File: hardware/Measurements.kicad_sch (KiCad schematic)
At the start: 4 parts, among them IC1 MCP1501-10E_SN

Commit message: minor changes
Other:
- note removed: "first stage lowpass filter"
- note removed: "second stage lowpass filter"
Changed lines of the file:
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@@
     (effects (font (size 5 5) (thickness 1) bold) (justify left bottom))
-  )
-  (text "second stage lowpass filter" (at 107.95 146.05 0)
-    (effects (font (size 1.27 1.27)) (justify left bottom))
   )
   (text "Sensor Reference" (at 198.755 29.21 0)
@@
     (effects (font (size 5 5) (thickness 1) bold) (justify left bottom))
   )
-  (text "first stage lowpass filter" (at 59.055 146.05 0)
-    (effects (font (size 1.27 1.27)) (justify left bottom))
-  )
   (global_label "HV_CAR+" (shape input) (at 74.295 74.295 180) (fields_autoplaced)

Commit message: pcb update
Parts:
- gave numbers to parts that had none: 1
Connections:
- net CUR_SENS_SIG: now also IC6.3 (+); no longer IC6.1 (NC)
- net SENSOR_SIGNAL_MCU: now also IC6.1; no longer IC6.2
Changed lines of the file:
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@@
   (symbol (lib_id "ADA4505-1ARJZ-R7:ADA4505-1ARJZ-R7") (at 86.995 162.56 0) (unit 1)
     (in_bom yes) (on_board yes)
-    (property "Reference" "IC?" (id 0) (at 94.615 155.575 0))
+    (property "Reference" "IC6" (id 0) (at 94.615 155.575 0))
     (property "Value" "ADA4505-1ARJZ-R7" (id 1) (at 99.06 157.48 0))
     (property "Footprint" "SOT95P280X145-5N" (id 2) (at 108.585 160.02 0)
@@
       (effects (font (size 1.27 1.27)) (justify left) hide)
     )
-    (pin "1")
+    (pin "3")
     (pin "1")
     (pin "2")
-    (pin "2")
+    (pin "1")
     (pin "4")
     (pin "5")
@@
   (symbol (lib_id "power:GND") (at 85.725 172.72 0) (unit 1)
     (in_bom yes) (on_board yes)
-    (property "Reference" "#PWR?" (id 0) (at 85.725 179.07 0)
+    (property "Reference" "#PWR0183" (id 0) (at 85.725 179.07 0)
       (effects (font (size 1.27 1.27)) hide)
     )
@@
   (symbol (lib_id "power:+3.3V") (at 85.725 152.4 0) (unit 1)
     (in_bom yes) (on_board yes)
-    (property "Reference" "#PWR?" (id 0) (at 85.725 156.21 0)
+    (property "Reference" "#PWR0182" (id 0) (at 85.725 156.21 0)
       (effects (font (size 1.27 1.27)) hide)
     )

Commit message: schemat sync
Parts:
- added C1, C2: 100nF, Capacitor_SMD:C_0603_1608Metric, symbol Device:C_Small
- added C6, C8: 1nF, Capacitor_SMD:C_0603_1608Metric, symbol Device:C_Small
- added IC7: MCP3562T-E_NC, QFN40P300X300X60-21N-D, symbol MCP3562T-E_NC:MCP3562T-E_NC
- added IC8: REF196GSZ-REEL, SOIC127P600X175-8N, symbol REF196GSZ-REEL:REF196GSZ-REEL
- added L1: 6.8uH, Inductor_SMD:L_1206_3216Metric, symbol Device:L
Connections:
- net SENSOR_SIGNAL_MCU is gone; now on net SIG: IC6.1, IC6.4 (-)
- net +3V3: now also C1.1, C2.1, IC7.18 (DVDD), L1.1
- net CUR_SENS_REF: now also IC7.5 (CH2)
- net GND: now also C1.2, C2.2, C6.2, C8.1, IC7.1 (REFIN-), IC7.17 (DGND), IC7.20 (AGND), IC7.21 (EP), IC7.4 (CH1), IC7.6 (CH3), IC8.4 (GND)
- net SCK: now also IC7.12 (SCK)
- net SDI: now also IC7.13 (SDI)
- net SDO: now also IC7.14 (SDO)
- net SIG: now reaches IC6.1
- net SIG: now also IC7.3 (CH0)
- new net: IC7.19 (AVDD), L1.2
- new net +5V: C6.1, IC8.2 (VSS), IC8.3 (~{SLEEP})
- new net 3.3V_REF: C8.2, IC7.2 (REFIN+), IC8.6 (REF_OUT)
- new net ~{SENS_CS}: IC7.11 (~{CS})
- no-connect marks 0 -> 2
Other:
- note added: "MCP35621T can be used for current sens signal measurements only"
- moved on the sheet: C4, C5, IC6

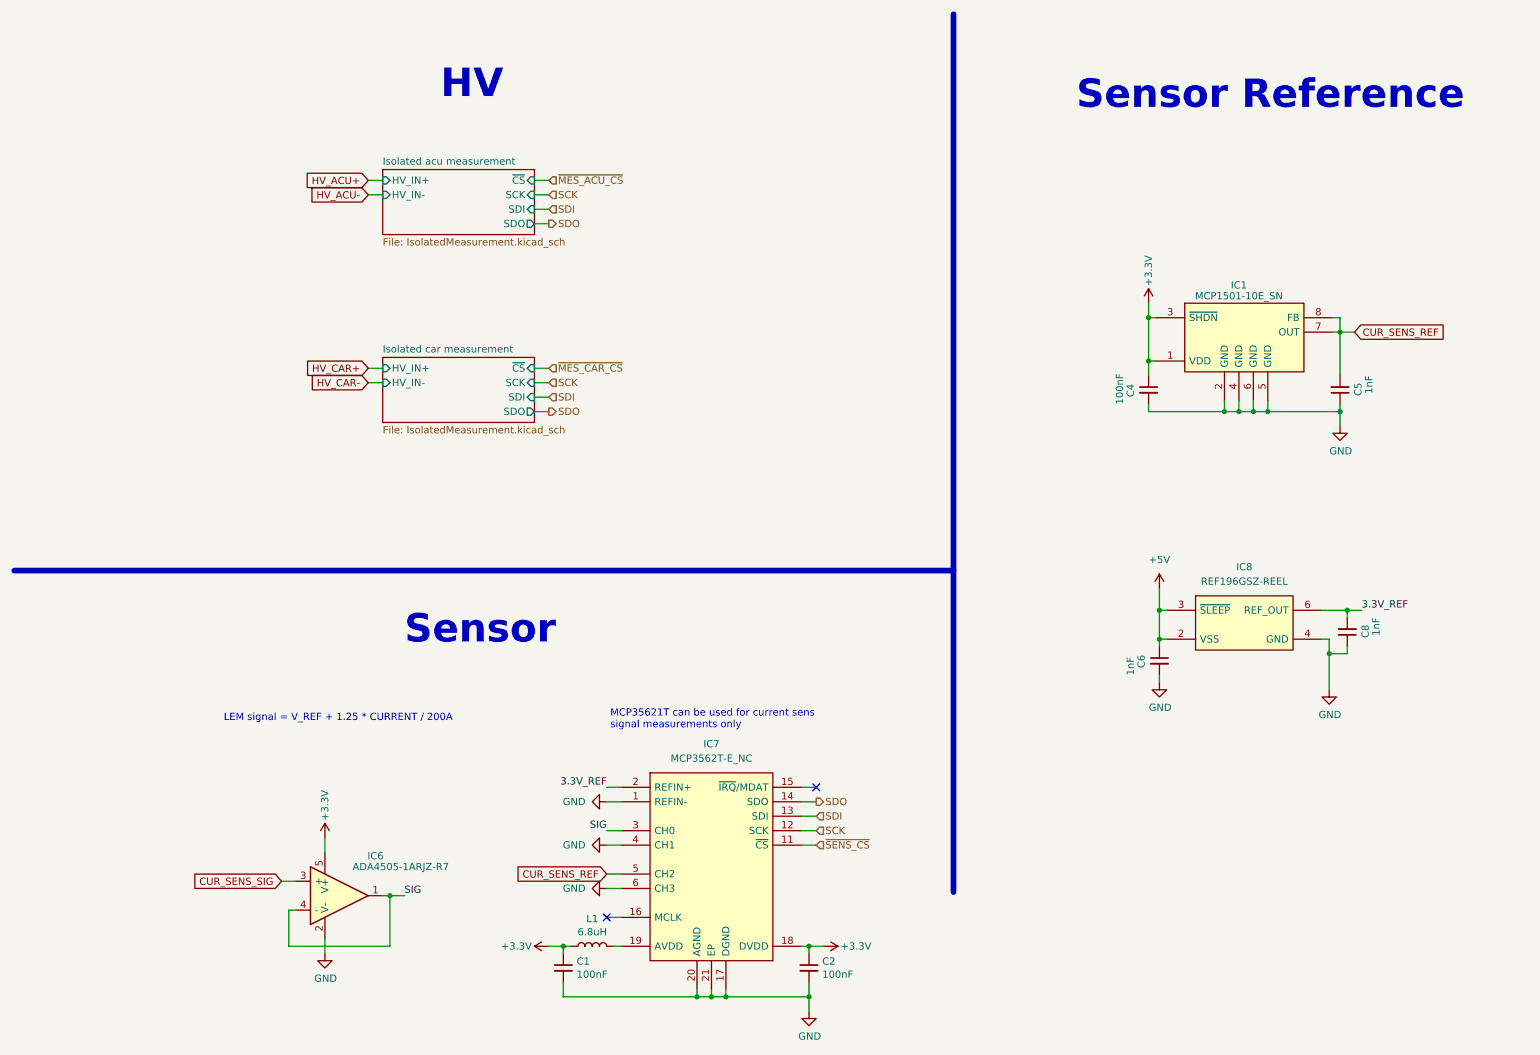
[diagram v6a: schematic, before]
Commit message: board sync and measurments section adjustments
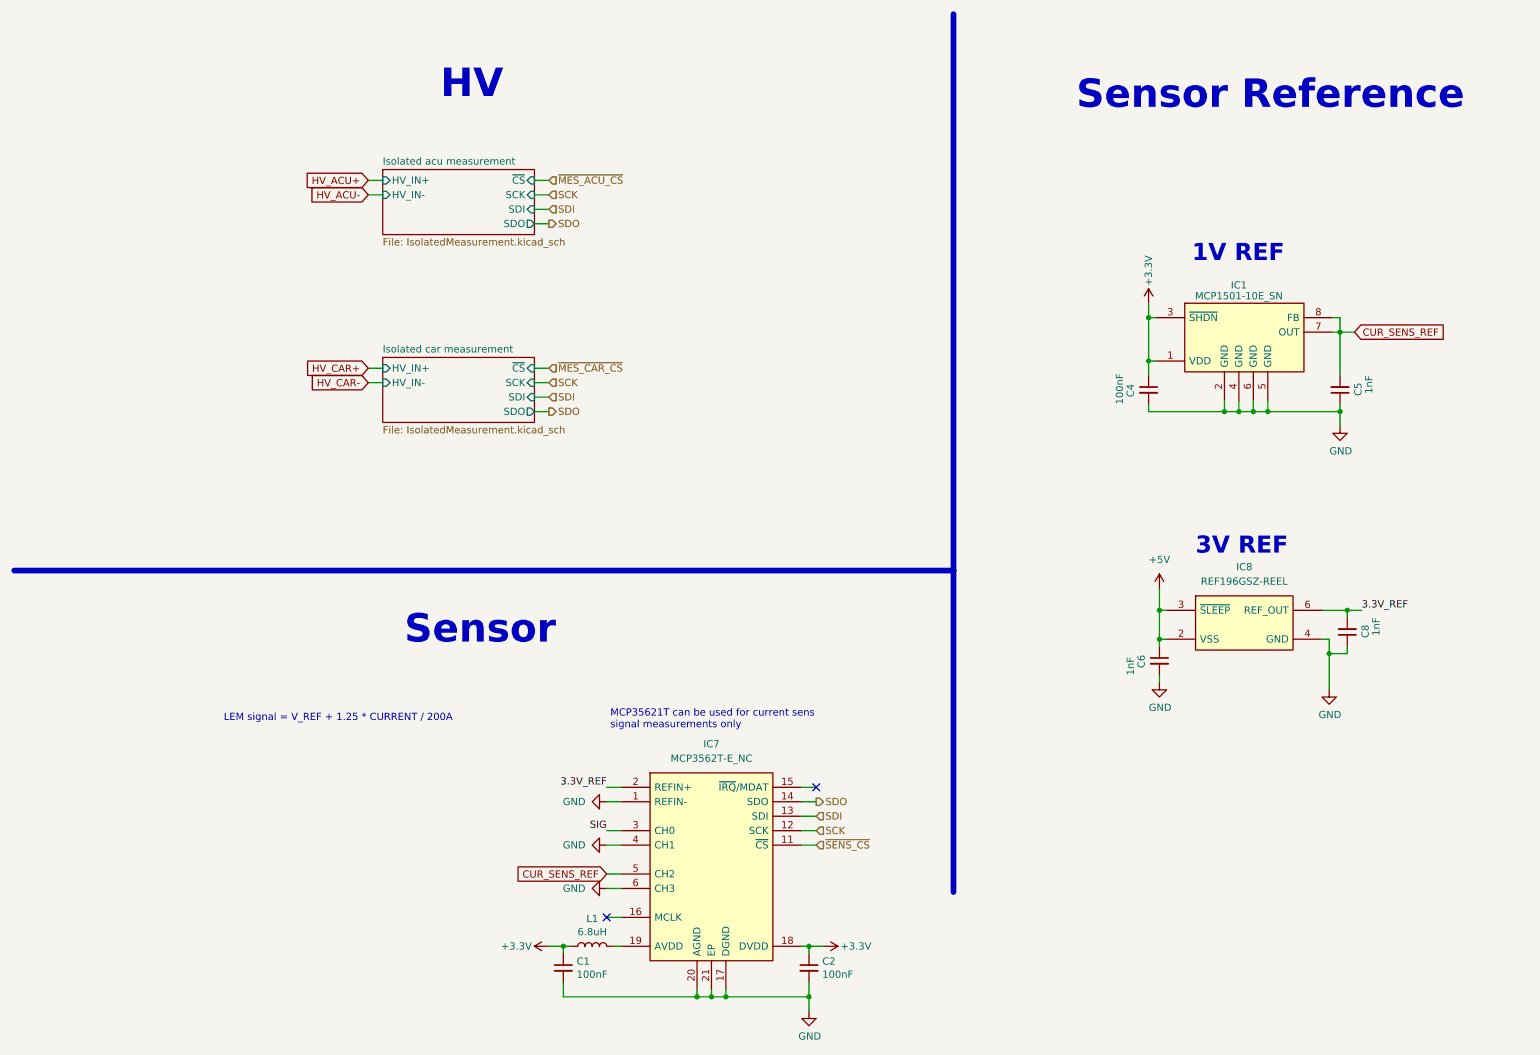
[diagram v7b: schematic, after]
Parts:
- removed IC6: ADA4505-1ARJZ-R7, SOT95P280X145-5N, symbol ADA4505-1ARJZ-R7:ADA4505-1ARJZ-R7
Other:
- note added: "1V REF"
- note added: "3V REF"
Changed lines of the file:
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@@
   (junction (at 229.87 81.915) (diameter 0) (color 0 0 0 0)
-  )
-  (junction (at 78.105 167.005) (diameter 0) (color 0 0 0 0)
   )
   (junction (at 245.11 67.945) (diameter 0) (color 0 0 0 0)
@@
     (stroke (width 0) (type default) (color 0 0 0 0))
   )
-  (wire (pts (xy 66.675 156.845) (xy 66.675 159.385))
-    (stroke (width 0) (type default) (color 0 0 0 0))
-  )
   (wire (pts (xy 150.495 147.955) (xy 153.035 147.955))
     (stroke (width 0) (type default) (color 0 0 0 0))
@@
     (stroke (width 0) (type default) (color 0 0 0 0))
   )
-  (wire (pts (xy 60.325 169.545) (xy 60.325 175.895))
-    (stroke (width 0) (type default) (color 0 0 0 0))
-  )
   (wire (pts (xy 227.33 81.915) (xy 227.33 80.01))
     (stroke (width 0) (type default) (color 0 0 0 0))
@@
   )
   (wire (pts (xy 106.045 175.895) (xy 108.585 175.895))
-    (stroke (width 0) (type default) (color 0 0 0 0))
-  )
-  (wire (pts (xy 80.645 167.005) (xy 78.105 167.005))
     (stroke (width 0) (type default) (color 0 0 0 0))
   )
@@
     (stroke (width 1) (type default) (color 132 0 0 1))
   )
-  (wire (pts (xy 61.595 169.545) (xy 60.325 169.545))
-    (stroke (width 0) (type default) (color 0 0 0 0))
-  )
   (wire (pts (xy 151.765 184.785) (xy 151.765 187.325))
     (stroke (width 0) (type default) (color 0 0 0 0))
@@
   )
   (wire (pts (xy 245.11 67.945) (xy 247.65 67.945))
-    (stroke (width 0) (type default) (color 0 0 0 0))
-  )
-  (wire (pts (xy 60.325 175.895) (xy 78.105 175.895))
     (stroke (width 0) (type default) (color 0 0 0 0))
   )
@@
     (stroke (width 0) (type default) (color 0 0 0 0))
   )
-  (wire (pts (xy 61.595 164.465) (xy 59.055 164.465))
-    (stroke (width 0) (type default) (color 0 0 0 0))
-  )
   (wire (pts (xy 211.455 73.025) (xy 211.455 75.565))
     (stroke (width 0) (type default) (color 0 0 0 0))
@@
     (stroke (width 0) (type default) (color 0 0 0 0))
   )
-  (wire (pts (xy 78.105 167.005) (xy 76.835 167.005))
-    (stroke (width 0) (type default) (color 0 0 0 0))
-  )
   (wire (pts (xy 241.935 121.92) (xy 243.205 121.92))
     (stroke (width 0) (type default) (color 0 0 0 0))
@@
     (stroke (width 0) (type default) (color 0 0 0 0))
   )
-  (wire (pts (xy 78.105 167.005) (xy 78.105 175.895))
-    (stroke (width 0) (type default) (color 0 0 0 0))
-  )
   (wire (pts (xy 243.84 65.405) (xy 245.11 65.405))
-    (stroke (width 0) (type default) (color 0 0 0 0))
-  )
-  (wire (pts (xy 66.675 174.625) (xy 66.675 177.165))
     (stroke (width 0) (type default) (color 0 0 0 0))
   )
@@
     (effects (font (size 5 5) (thickness 1) bold) (justify left bottom))
   )
-  (label "SIG" (at 80.645 167.005 0)
-    (effects (font (size 1.27 1.27)) (justify left bottom))
+  (text "1V REF\n" (at 219.075 55.88 0)
+    (effects (font (size 3 3) (thickness 1) bold) (justify left bottom))
+  )
+  (text "3V REF\n" (at 219.71 107.315 0)
+    (effects (font (size 3 3) (thickness 1) bold) (justify left bottom))
   )
   (label "3.3V_REF" (at 248.92 116.84 0)
@@
     (effects (font (size 1.27 1.27)) (justify right))
     (property "Intersheet References" "${INTERSHEET_REFS}" (id 0) (at 63.3832 76.7556 0)
-      (effects (font (size 1.27 1.27)) (justify right) hide)
-    )
-  )
-  (global_label "CUR_SENS_SIG" (shape input) (at 59.055 164.465 180) (fields_autoplaced)
-    (effects (font (size 1.27 1.27)) (justify right))
-    (property "Intersheet References" "${INTERSHEET_REFS}" (id 0) (at 42.9422 164.3856 0)
       (effects (font (size 1.27 1.27)) (justify right) hide)
     )
@@
     (pin "8")
   )
-  (symbol (lib_id "ADA4505-1ARJZ-R7:ADA4505-1ARJZ-R7") (at 67.945 167.005 0) (unit 1)
-    (in_bom yes) (on_board yes)
-    (property "Reference" "IC6" (id 0) (at 75.565 160.02 0))
-    (property "Value" "ADA4505-1ARJZ-R7" (id 1) (at 80.01 161.925 0))
-    (property "Footprint" "SOT95P280X145-5N" (id 2) (at 89.535 164.465 0)
-      (effects (font (size 1.27 1.27)) (justify left) hide)
-    )
-    (property "Datasheet" "https://componentsearchengine.com/Datasheets/5/ADA4505-1ARJZ-R7.pdf" (id 3) (at 89.535 167.005 0)
-      (effects (font (size 1.27 1.27)) (justify left) hide)
-    )
-    (property "Description" "10 A, Rail-to-Rail I/O, Zero Input  Crossover Distortion Amplifiers" (id 4) (at 89.535 169.545 0)
-      (effects (font (size 1.27 1.27)) (justify left) hide)
-    )
-    (property "Height" "1.45" (id 5) (at 89.535 172.085 0)
-      (effects (font (size 1.27 1.27)) (justify left) hide)
-    )
-    (property "Mouser Part Number" "584-ADA4505-1ARJZ-R7" (id 6) (at 89.535 174.625 0)
-      (effects (font (size 1.27 1.27)) (justify left) hide)
-    )
-    (property "Mouser Price/Stock" "https://www.mouser.co.uk/ProductDetail/Analog-Devices/ADA4505-1ARJZ-R7?qs=BpaRKvA4VqHv2LvIinabEg%3D%3D" (id 7) (at 89.535 177.165 0)
-      (effects (font (size 1.27 1.27)) (justify left) hide)
-    )
-    (property "Manufacturer_Name" "Analog Devices" (id 8) (at 89.535 179.705 0)
-      (effects (font (size 1.27 1.27)) (justify left) hide)
-    )
-    (property "Manufacturer_Part_Number" "ADA4505-1ARJZ-R7" (id 9) (at 89.535 182.245 0)
-      (effects (font (size 1.27 1.27)) (justify left) hide)
-    )
-    (pin "1")
-    (pin "1")
-    (pin "2")
-    (pin "3")
-    (pin "4")
-    (pin "5")
-    (pin "5")
-    (pin "8")
-  )
   (symbol (lib_id "power:GND") (at 116.205 150.495 270) (unit 1)
     (in_bom yes) (on_board yes)
@@
     )
     (property "Datasheet" "" (id 3) (at 116.205 150.495 0)
-      (effects (font (size 1.27 1.27)) hide)
-    )
-    (pin "1")
-  )
-  (symbol (lib_id "power:GND") (at 66.675 177.165 0) (unit 1)
-    (in_bom yes) (on_board yes)
-    (property "Reference" "#PWR0183" (id 0) (at 66.675 183.515 0)
-      (effects (font (size 1.27 1.27)) hide)
-    )
-    (property "Value" "GND" (id 1) (at 66.802 181.5592 0))
-    (property "Footprint" "" (id 2) (at 66.675 177.165 0)
-      (effects (font (size 1.27 1.27)) hide)
-    )
-    (property "Datasheet" "" (id 3) (at 66.675 177.165 0)
       (effects (font (size 1.27 1.27)) hide)
     )
@@
       (effects (font (size 1.27 1.27)) hide)
     )
-    (pin "1")
-  )
-  (symbol (lib_id "power:+3.3V") (at 66.675 156.845 0) (unit 1)
-    (in_bom yes) (on_board yes)
-    (property "Reference" "#PWR0182" (id 0) (at 66.675 160.655 0)
-      (effects (font (size 1.27 1.27)) hide)
-    )
-    (property "Value" "+3.3V" (id 1) (at 66.675 151.13 90))
-    (property "Footprint" "" (id 2) (at 66.675 156.845 0)
-      (effects (font (size 1.27 1.27)) hide)
-    )
-    (property "Datasheet" "" (id 3) (at 66.675 156.845 0)
-      (effects (font (size 1.27 1.27)) hide)
-    )
